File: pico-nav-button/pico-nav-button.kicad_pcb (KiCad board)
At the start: 2 copper layers, 29.5 x 11.2 mm, 4 parts, among them J1 Conn_01x04, J2 Conn_01x04, U1 Nav_Button, U2 Slider

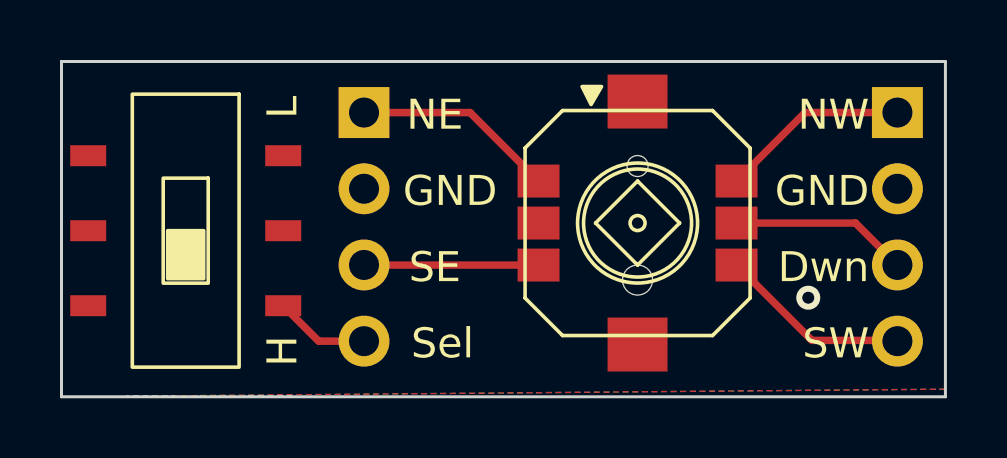
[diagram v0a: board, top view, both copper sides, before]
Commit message: Rev 1.10: fixed pad-to-pin assignments
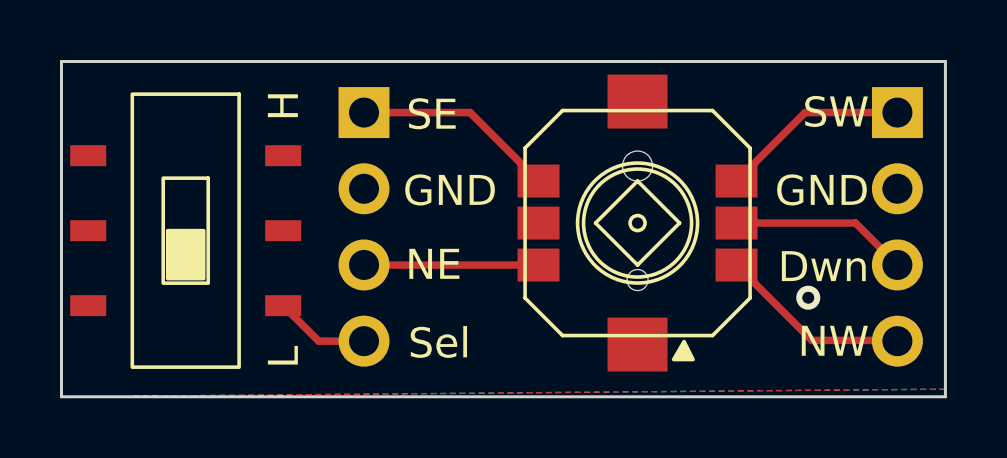
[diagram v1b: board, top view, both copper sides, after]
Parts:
- turned U1 to 0 degrees
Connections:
- J1 pad 1: /NW -> /SW
- J1 pad 4: /SW -> /NW
- J2 pad 1: /NE -> /SE
- J2 pad 3: /SE -> /NE
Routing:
- net /SE: track 5.82 -> 6.76 mm
- net /NE: track 6.76 -> 5.82 mm
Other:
- board text added: "Rev. 1.10"
- board text removed: "Rev. 1.00"
